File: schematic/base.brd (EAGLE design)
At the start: 100 x 80 mm, 10 parts, among them Q1 BC557, Q2 BC557

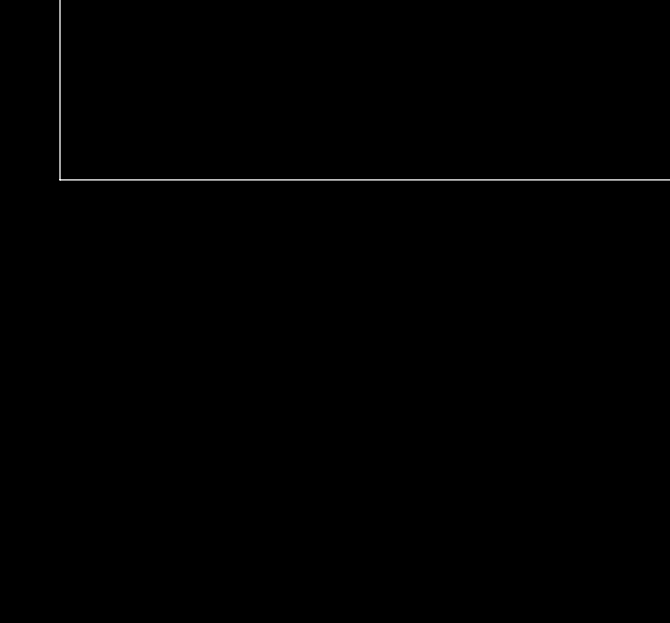
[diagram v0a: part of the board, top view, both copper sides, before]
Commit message: Add DHT to sematic
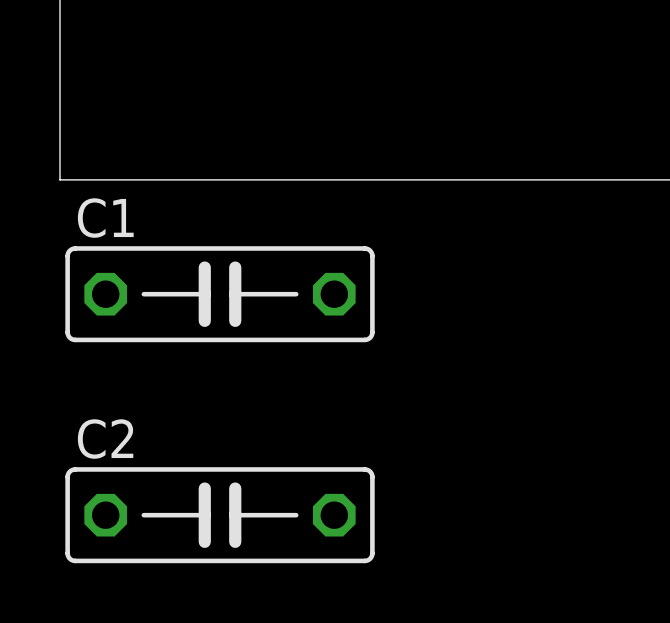
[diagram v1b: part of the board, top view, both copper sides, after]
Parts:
- added C1, C2: 10n, rcl:C075-032X103
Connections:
- net +3V3: now also C1.1, C2.1
- net N$4: now also C2.2
- net N$5: now also C1.2
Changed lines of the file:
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@@
 </element>
 <element name="R4" library="rcl" package="0204/7" value="2k2" x="15.24" y="16.51" rot="R270"/>
+<element name="C1" library="rcl" package="C075-032X103" value="10n" x="5.334" y="-3.81"/>
+<element name="C2" library="rcl" package="C075-032X103" value="10n" x="5.334" y="-11.176"/>
 </elements>
 <signals>
@@
 <contactref element="Q1" pad="E"/>
 <contactref element="Q2" pad="E"/>
-<contactref element="SHAFT_ENCODER" pad="1"/>
 <contactref element="AM2303" pad="1"/>
 <wire x1="20.32" y1="27.94" x2="20.32" y2="20.32" width="0.4064" layer="16"/>
@@
 <wire x1="20.32" y1="33.02" x2="7.62" y2="33.02" width="0.4064" layer="16"/>
 <wire x1="7.62" y1="33.02" x2="7.62" y2="25.4" width="0.4064" layer="16"/>
-<wire x1="7.62" y1="17.78" x2="17.78" y2="17.78" width="0" layer="19" extent="16-16"/>
-<wire x1="33.02" y1="17.78" x2="20.32" y2="17.78" width="0" layer="19" extent="16-16"/>
+<contactref element="C1" pad="1"/>
+<contactref element="C2" pad="1"/>
+<contactref element="SHAFT_ENCODER" pad="1"/>
+<wire x1="20.32" y1="17.78" x2="33.02" y2="17.78" width="0" layer="19" extent="16-16"/>
+<wire x1="17.78" y1="17.78" x2="20.32" y2="17.78" width="0" layer="19" extent="16-16"/>
+<wire x1="1.524" y1="-3.81" x2="7.62" y2="17.78" width="0" layer="19" extent="16-16"/>
+<wire x1="1.524" y1="-11.176" x2="1.524" y2="-3.81" width="0" layer="19" extent="1-1"/>
 </signal>
 <signal name="N$1">
@@
 <contactref element="Q2" pad="C"/>
 <contactref element="SHAFT_ENCODER" pad="2"/>
+<contactref element="C2" pad="2"/>
 <wire x1="25.4" y1="20.32" x2="33.02" y2="20.32" width="0" layer="19" extent="1-1"/>
+<wire x1="9.144" y1="-11.176" x2="25.4" y2="20.32" width="0" layer="19" extent="1-1"/>
 </signal>
 <signal name="N$5">
 <contactref element="SHAFT_ENCODER" pad="3"/>
 <contactref element="Q1" pad="C"/>
+<contactref element="C1" pad="2"/>
 <wire x1="25.4" y1="27.94" x2="33.02" y2="22.86" width="0" layer="19" extent="1-1"/>
+<wire x1="9.144" y1="-3.81" x2="25.4" y2="27.94" width="0" layer="19" extent="1-1"/>
 </signal>
 <signal name="N$6">
